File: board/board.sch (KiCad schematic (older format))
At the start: 29 parts, among them J1 Conn_02x03_Odd_Even, J3 RPi_GPIO, SW1 SW_Push, SW2 SW_Push, SW3 SW_Push, SW4 SW_Push

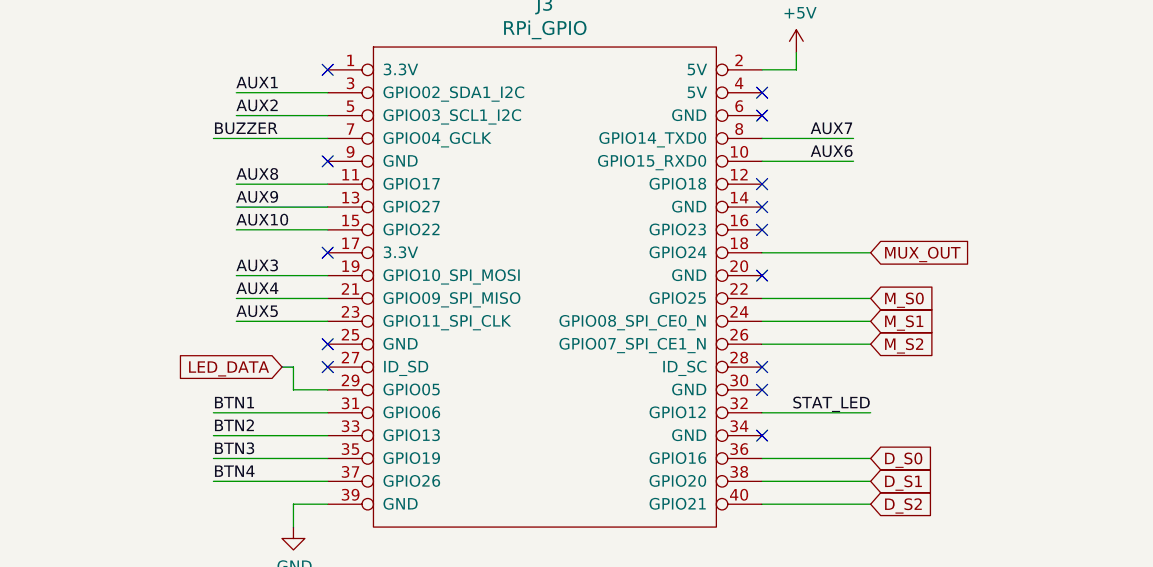
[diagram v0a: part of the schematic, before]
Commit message: WS2812B test code added
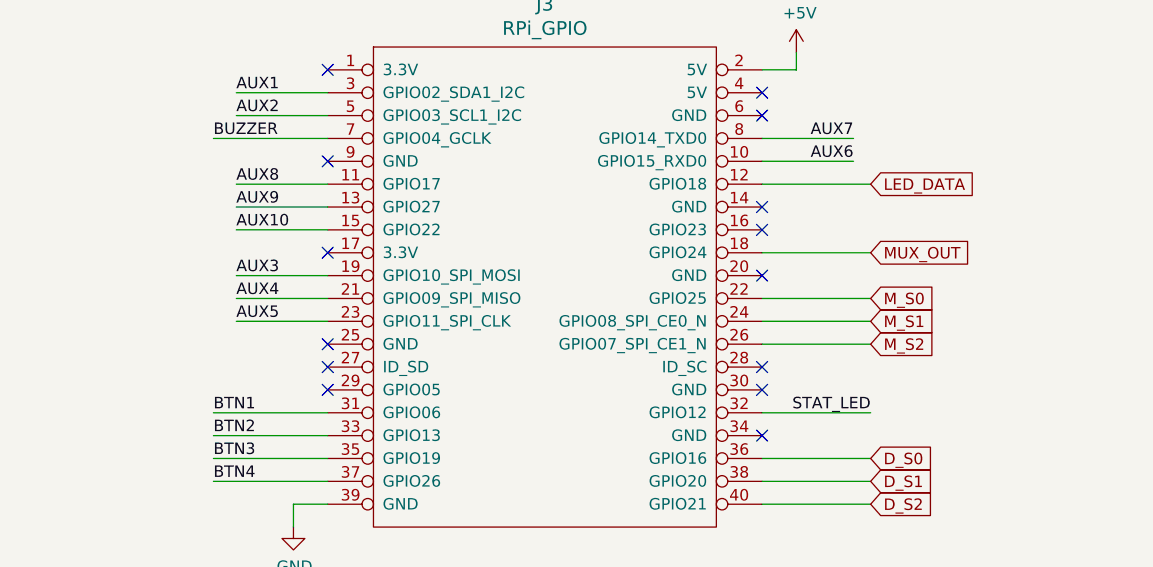
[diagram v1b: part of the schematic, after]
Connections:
- net LED_DATA: now also J3.12 (GPIO18); no longer J3.29 (GPIO05)
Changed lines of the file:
@@
 F1 "hall.sch" 50
 $EndSheet
-Wire Wire Line
-	4775 2925 4925 2925
 NoConn ~ 6825 2225
-NoConn ~ 6825 2025
 $Comp
 L board:RPi_GPIO J3
@@
 Wire Wire Line
 	7225 1925 6825 1925
-Text GLabel 4725 2825 0    50   Input ~ 0
+Text GLabel 7300 2025 2    50   Input ~ 0
 LED_DATA
 Text Label 4425 3025 0    50   ~ 0
 BTN1
-Wire Wire Line
-	4725 2825 4775 2825
-Wire Wire Line
-	4775 2825 4775 2925
 Wire Wire Line
 	4425 3225 4925 3225
@@
 Text Label 5500 4950 2    50   ~ 0
 AUX10
+NoConn ~ 4925 2925
+Wire Wire Line
+	6825 2025 7300 2025
 $EndSCHEMATC

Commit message: PCB: Minor changes
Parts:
- removed J1: Conn_02x03_Odd_Even, Connector_PinHeader_2.54mm:PinHeader_2x03_P2.54mm_Vertical, symbol Connector_Generic:Conn_02x03_Odd_Even
- added J1: Conn_01x02_Female, Connector_JST:JST_XH_B2B-XH-A_1x02_P2.50mm_Vertical, symbol Connector:Conn_01x02_Female
- C1: footprint Capacitor_THT:C_Radial_D6.3mm_H11.0mm_P2.50mm -> Capacitor_SMD:C_0805_2012Metric_Pad1.18x1.45mm_HandSolder
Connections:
- net +5V: now also J1.1 (Pin_1)
- net GND: now also J1.2 (Pin_2)
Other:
- moved on the sheet: J3
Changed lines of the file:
@@
 EESchema Schematic File Version 4
-LIBS:board-cache
 EELAYER 30 0
 EELAYER END
@@
 Wire Wire Line
 	2475 5900 2475 6150
-Text Label 4425 3125 0    50   ~ 0
+Text Label 4450 2850 0    50   ~ 0
 BTN2
-Text Label 7300 3025 2    50   ~ 0
+Text Label 7325 2750 2    50   ~ 0
 STAT_LED
-Text Label 4425 1825 0    50   ~ 0
+Text Label 4450 1550 0    50   ~ 0
 BUZZER
 Wire Wire Line
-	4925 3025 4425 3025
+	4950 2750 4450 2750
 Text Label 1475 4925 3    50   ~ 0
 BTN1
@@
 F 0 "C1" H 3167 1196 50  0000 L CNN
 F 1 "2.2uF" H 3167 1105 50  0000 L CNN
-F 2 "Capacitor_THT:C_Radial_D6.3mm_H11.0mm_P2.50mm" H 3075 1150 50  0001 C CNN
+F 2 "Capacitor_SMD:C_0805_2012Metric_Pad1.18x1.45mm_HandSolder" H 3075 1150 50  0001 C CNN
 F 3 "~" H 3075 1150 50  0001 C CNN
 	1    3075 1150
@@
 	3075 975  3075 1050
 Wire Wire Line
-	6825 1525 6975 1525
-Wire Wire Line
-	6975 1525 6975 1450
-NoConn ~ 6825 1625
-NoConn ~ 4925 1525
-NoConn ~ 4925 2325
-NoConn ~ 4925 1925
-NoConn ~ 6825 2125
-NoConn ~ 6825 2425
-NoConn ~ 6825 2925
-NoConn ~ 6825 3125
-NoConn ~ 6825 1725
-NoConn ~ 4925 2725
+	6850 1250 7000 1250
+Wire Wire Line
+	7000 1250 7000 1175
+NoConn ~ 6850 1350
+NoConn ~ 4950 1250
+NoConn ~ 4950 2050
+NoConn ~ 4950 1650
+NoConn ~ 6850 1850
+NoConn ~ 6850 2150
+NoConn ~ 6850 2650
+NoConn ~ 6850 2850
+NoConn ~ 6850 1450
+NoConn ~ 4950 2450
 $Comp
 L power:GND #PWR011
 U 1 1 5FD9644A
-P 4775 3525
-F 0 "#PWR011" H 4775 3275 50  0001 C CNN
-F 1 "GND" H 4780 3352 50  0000 C CNN
-F 2 "" H 4775 3525 50  0001 C CNN
-F 3 "" H 4775 3525 50  0001 C CNN
-	1    4775 3525
+P 4800 3250
+F 0 "#PWR011" H 4800 3000 50  0001 C CNN
+F 1 "GND" H 4805 3077 50  0000 C CNN
+F 2 "" H 4800 3250 50  0001 C CNN
+F 3 "" H 4800 3250 50  0001 C CNN
+	1    4800 3250
 	1    0    0    -1
 $EndComp
@@
 L power:+5V #PWR013
 U 1 1 5FD97EE7
-P 6975 1450
-F 0 "#PWR013" H 6975 1300 50  0001 C CNN
-F 1 "+5V" H 6990 1623 50  0000 C CNN
-F 2 "" H 6975 1450 50  0001 C CNN
-F 3 "" H 6975 1450 50  0001 C CNN
-	1    6975 1450
-	1    0    0    -1
-$EndComp
-Wire Wire Line
-	4925 1825 4425 1825
-Wire Wire Line
-	6825 2325 7300 2325
-Wire Wire Line
-	6825 2525 7300 2525
-Wire Wire Line
-	6825 2625 7300 2625
-Wire Wire Line
-	6825 2725 7300 2725
-Wire Wire Line
-	6825 3025 7300 3025
-Wire Wire Line
-	6825 3225 7300 3225
-Wire Wire Line
-	6825 3325 7300 3325
-Wire Wire Line
-	6825 3425 7300 3425
+P 7000 1175
+F 0 "#PWR013" H 7000 1025 50  0001 C CNN
+F 1 "+5V" H 7015 1348 50  0000 C CNN
+F 2 "" H 7000 1175 50  0001 C CNN
+F 3 "" H 7000 1175 50  0001 C CNN
+	1    7000 1175
+	1    0    0    -1
+$EndComp
+Wire Wire Line
+	4950 1550 4450 1550
+Wire Wire Line
+	6850 2050 7325 2050
+Wire Wire Line
+	6850 2250 7325 2250
+Wire Wire Line
+	6850 2350 7325 2350
+Wire Wire Line
+	6850 2450 7325 2450
+Wire Wire Line
+	6850 2750 7325 2750
+Wire Wire Line
+	6850 2950 7325 2950
+Wire Wire Line
+	6850 3050 7325 3050
+Wire Wire Line
+	6850 3150 7325 3150
 $Comp
 L Switch:SW_Push SW3
@@
 Wire Wire Line
 	2000 4950 2000 5500
-Text GLabel 7300 2325 2    50   Input ~ 0
+Text GLabel 7325 2050 2    50   Input ~ 0
 MUX_OUT
-Text GLabel 7300 2525 2    50   Input ~ 0
+Text GLabel 7325 2250 2    50   Input ~ 0
 M_S0
-Text GLabel 7300 2625 2    50   Input ~ 0
+Text GLabel 7325 2350 2    50   Input ~ 0
 M_S1
-Text GLabel 7300 2725 2    50   Input ~ 0
+Text GLabel 7325 2450 2    50   Input ~ 0
 M_S2
 Wire Wire Line
-	4425 3125 4925 3125
-Text GLabel 7300 3225 2    50   Input ~ 0
+	4450 2850 4950 2850
+Text GLabel 7325 2950 2    50   Input ~ 0
 D_S0
-Text GLabel 7300 3325 2    50   Input ~ 0
+Text GLabel 7325 3050 2    50   Input ~ 0
 D_S1
-Text GLabel 7300 3425 2    50   Input ~ 0
+Text GLabel 7325 3150 2    50   Input ~ 0
 D_S2
 Wire Wire Line
-	4925 2425 4525 2425
-Wire Wire Line
-	4925 2525 4525 2525
-Wire Wire Line
-	4925 2625 4525 2625
-Wire Wire Line
-	4925 1625 4525 1625
-Wire Wire Line
-	4925 1725 4525 1725
-Text Label 4525 1625 0    50   ~ 0
+	4950 2150 4550 2150
+Wire Wire Line
+	4950 2250 4550 2250
+Wire Wire Line
+	4950 2350 4550 2350
+Wire Wire Line
+	4950 1350 4550 1350
+Wire Wire Line
+	4950 1450 4550 1450
+Text Label 4550 1350 0    50   ~ 0
 AUX1
-Text Label 4525 1725 0    50   ~ 0
+Text Label 4550 1450 0    50   ~ 0
 AUX2
-Text Label 4525 2425 0    50   ~ 0
+Text Label 4550 2150 0    50   ~ 0
 AUX3
-Text Label 4525 2525 0    50   ~ 0
+Text Label 4550 2250 0    50   ~ 0
 AUX4
-Text Label 4525 2625 0    50   ~ 0
+Text Label 4550 2350 0    50   ~ 0
 AUX5
 Text Notes 4775 5125 0    50   ~ 0
@@
 	1    0    0    -1
 $EndComp
-$Comp
-L Connector_Generic:Conn_02x03_Odd_Even J1
-U 1 1 60115434
-P 4775 6200
-F 0 "J1" H 4825 6517 50  0000 C CNN
-F 1 "Conn_02x03_Odd_Even" H 4825 6426 50  0000 C CNN
-F 2 "Connector_PinHeader_2.54mm:PinHeader_2x03_P2.54mm_Vertical" H 4775 6200 50  0001 C CNN
-F 3 "~" H 4775 6200 50  0001 C CNN
-	1    4775 6200
-	1    0    0    -1
-$EndComp
-Wire Wire Line
-	4575 6100 4250 6100
-Wire Wire Line
-	4575 6200 4250 6200
-Wire Wire Line
-	4575 6300 4250 6300
-Wire Wire Line
-	5400 6100 5075 6100
-Wire Wire Line
-	5400 6200 5075 6200
-Wire Wire Line
-	5400 6300 5075 6300
-Wire Wire Line
-	4250 6300 4250 6200
-Wire Wire Line
-	4250 6100 4250 6200
-Connection ~ 4250 6200
-Wire Wire Line
-	5400 6100 5400 6200
-Connection ~ 5400 6200
-Wire Wire Line
-	5400 6200 5400 6300
-Connection ~ 5400 6300
-Wire Wire Line
-	5400 6300 5400 6375
-Wire Wire Line
-	4250 6100 4250 6025
-Connection ~ 4250 6100
+Wire Wire Line
+	4800 6050 4475 6050
+Wire Wire Line
+	4800 6150 4475 6150
+Wire Wire Line
+	4475 6150 4475 6225
+Wire Wire Line
+	4475 6050 4475 5975
 $Comp
 L power:GND #PWR012
 U 1 1 60123738
-P 5400 6375
-F 0 "#PWR012" H 5400 6125 50  0001 C CNN
-F 1 "GND" H 5405 6202 50  0000 C CNN
-F 2 "" H 5400 6375 50  0001 C CNN
-F 3 "" H 5400 6375 50  0001 C CNN
-	1    5400 6375
+P 4475 6225
+F 0 "#PWR012" H 4475 5975 50  0001 C CNN
+F 1 "GND" H 4480 6052 50  0000 C CNN
+F 2 "" H 4475 6225 50  0001 C CNN
+F 3 "" H 4475 6225 50  0001 C CNN
+	1    4475 6225
 	1    0    0    -1
 $EndComp
@@
 L power:+5V #PWR010
 U 1 1 60123BEB
-P 4250 6025
-F 0 "#PWR010" H 4250 5875 50  0001 C CNN
-F 1 "+5V" H 4265 6198 50  0000 C CNN
-F 2 "" H 4250 6025 50  0001 C CNN
-F 3 "" H 4250 6025 50  0001 C CNN
-	1    4250 6025
-	1    0    0    -1
-$EndComp
-NoConn ~ 6825 2825
-NoConn ~ 4925 2825
+P 4475 5975
+F 0 "#PWR010" H 4475 5825 50  0001 C CNN
+F 1 "+5V" H 4490 6148 50  0000 C CNN
+F 2 "" H 4475 5975 50  0001 C CNN
+F 3 "" H 4475 5975 50  0001 C CNN
+	1    4475 5975
+	1    0    0    -1
+$EndComp
+NoConn ~ 6850 2550
+NoConn ~ 4950 2550
 Wire Wire Line
 	5100 4550 5500 4550
@@
 F1 "hall.sch" 50
 $EndSheet
-NoConn ~ 6825 2225
+NoConn ~ 6850 1950
 $Comp
 L board:RPi_GPIO J3
 U 1 1 5FD50DA9
-P 5125 1525
-F 0 "J3" H 5875 1812 60  0000 C CNN
-F 1 "RPi_GPIO" H 5875 1706 60  0000 C CNN
-F 2 "board:raspberry_pi_socket" H 5125 1525 60  0001 C CNN
-F 3 "" H 5125 1525 60  0000 C CNN
-	1    5125 1525
+P 5150 1250
+F 0 "J3" H 5900 1537 60  0000 C CNN
+F 1 "RPi_GPIO" H 5900 1431 60  0000 C CNN
+F 2 "board:raspberry_pi_socket" H 5150 1250 60  0001 C CNN
+F 3 "" H 5150 1250 60  0000 C CNN
+	1    5150 1250
 	1    0    0    -1
 $EndComp
@@
 Wire Wire Line
 	2975 4950 2975 5500
-Text Label 7225 1925 2    50   ~ 0
+Text Label 7250 1650 2    50   ~ 0
 AUX6
 Wire Wire Line
-	4775 3425 4925 3425
-Wire Wire Line
-	4775 3525 4775 3425
-Wire Wire Line
-	7225 1925 6825 1925
-Text GLabel 7300 2025 2    50   Input ~ 0
+	4800 3150 4950 3150
+Wire Wire Line
+	4800 3250 4800 3150
+Wire Wire Line
+	7250 1650 6850 1650
+Text GLabel 7325 1750 2    50   Input ~ 0
 LED_DATA
-Text Label 4425 3025 0    50   ~ 0
+Text Label 4450 2750 0    50   ~ 0
 BTN1
 Wire Wire Line
-	4425 3225 4925 3225
-Text Label 4425 3225 0    50   ~ 0
+	4450 2950 4950 2950
+Text Label 4450 2950 0    50   ~ 0
 BTN3
 Wire Wire Line
-	4425 3325 4925 3325
-Text Label 4425 3325 0    50   ~ 0
+	4450 3050 4950 3050
+Text Label 4450 3050 0    50   ~ 0
 BTN4
-Text Label 7225 1825 2    50   ~ 0
+Text Label 7250 1550 2    50   ~ 0
 AUX7
 Wire Wire Line
-	7225 1825 6825 1825
-Text Label 4525 2025 0    50   ~ 0
+	7250 1550 6850 1550
+Text Label 4550 1750 0    50   ~ 0
 AUX8
 Wire Wire Line
-	4525 2025 4925 2025
-Text Label 4525 2125 0    50   ~ 0
+	4550 1750 4950 1750
+Text Label 4550 1850 0    50   ~ 0
 AUX9
 Wire Wire Line
-	4525 2125 4925 2125
-Text Label 4525 2225 0    50   ~ 0
+	4550 1850 4950 1850
+Text Label 4550 1950 0    50   ~ 0
 AUX10
 Wire Wire Line
-	4525 2225 4925 2225
+	4550 1950 4950 1950
 $Comp
 L Connector_Generic:Conn_02x05_Odd_Even e1
@@
 Text Label 5500 4950 2    50   ~ 0
 AUX10
-NoConn ~ 4925 2925
-Wire Wire Line
-	6825 2025 7300 2025
+NoConn ~ 4950 2650
+Wire Wire Line
+	6850 1750 7325 1750
+$Comp
+L Connector:Conn_01x02_Female J1
+U 1 1 6203770B
+P 5000 6050
+F 0 "J1" H 5028 6026 50  0000 L CNN
+F 1 "Conn_01x02_Female" V 5175 5625 50  0000 L CNN
+F 2 "Connector_JST:JST_XH_B2B-XH-A_1x02_P2.50mm_Vertical" H 5000 6050 50  0001 C CNN
+F 3 "~" H 5000 6050 50  0001 C CNN
+	1    5000 6050
+	1    0    0    -1
+$EndComp
 $EndSCHEMATC

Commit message: Folder reorganized: board
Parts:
- J3: footprint board:raspberry_pi_socket -> Board:raspberry_pi_socket; symbol board:RPi_GPIO -> Board:RPi_GPIO
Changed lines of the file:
@@
 NoConn ~ 6850 1950
 $Comp
-L board:RPi_GPIO J3
+L Board:RPi_GPIO J3
 U 1 1 5FD50DA9
 P 5150 1250
 F 0 "J3" H 5900 1537 60  0000 C CNN
 F 1 "RPi_GPIO" H 5900 1431 60  0000 C CNN
-F 2 "board:raspberry_pi_socket" H 5150 1250 60  0001 C CNN
+F 2 "Board:raspberry_pi_socket" H 5150 1250 60  0001 C CNN
 F 3 "" H 5150 1250 60  0000 C CNN
 	1    5150 1250
